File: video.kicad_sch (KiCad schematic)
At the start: 18 parts, among them Q1 BC547B, Q3 BC547B, Q4 BC547B, Q5 BC547B, Q6 BC547B

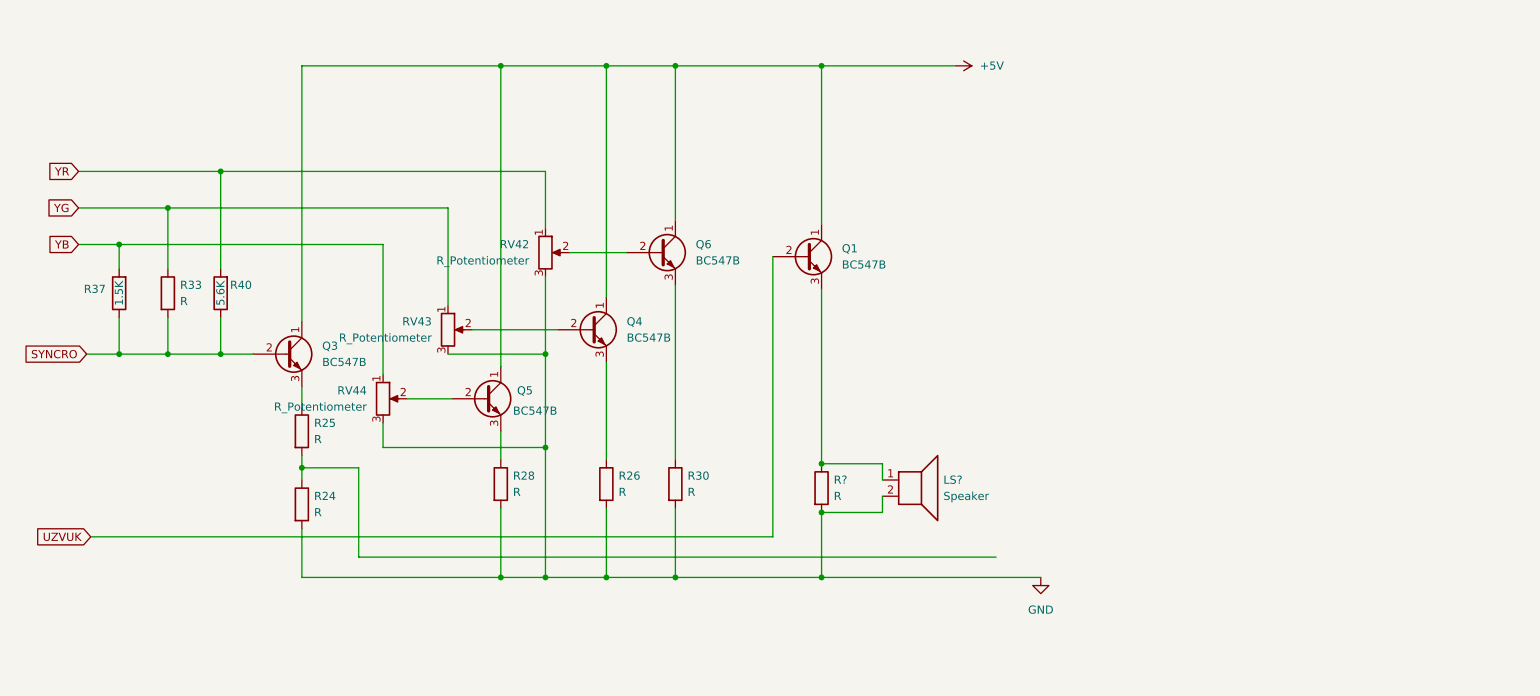
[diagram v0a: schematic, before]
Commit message: March 23rd First pre-alpha
First time ZERO errors and 93 warnings. Schematics are done, now to deal with warnings and footprints.
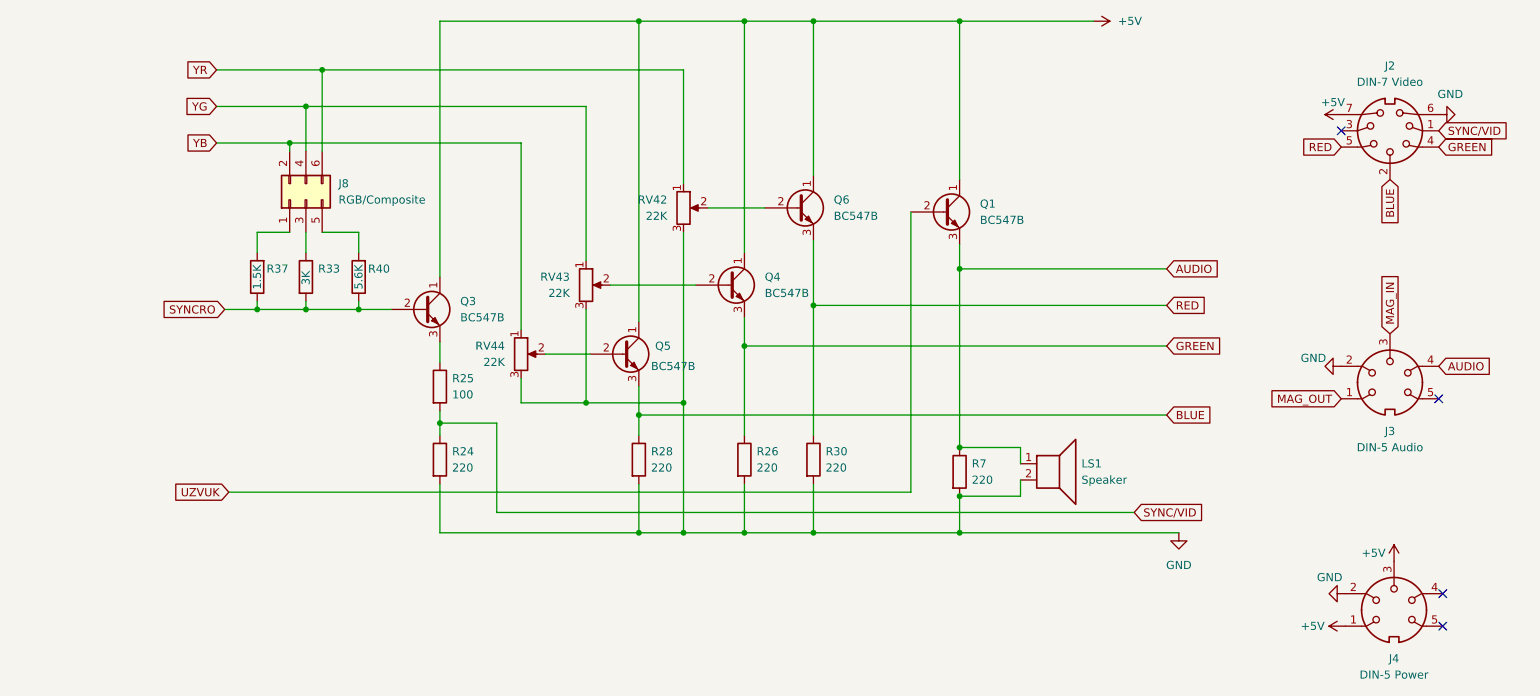
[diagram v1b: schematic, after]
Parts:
- added J2: DIN-7 Video, symbol Connector:DIN-7
- added J3: DIN-5 Audio, symbol Connector:DIN-5
- added J4: DIN-5 Power, symbol Connector:DIN-5
- added J8: RGB/Composite, Connector_PinHeader_2.54mm:PinHeader_2x03_P2.54mm_Vertical, symbol Connector_Generic:Conn_02x03_Odd_Even
- R24, R26, R28, R30: value R -> 220; footprint (none) -> Resistor_THT:R_Axial_DIN0207_L6.3mm_D2.5mm_P10.16mm_Horizontal
- R25: value R -> 100; footprint (none) -> Resistor_THT:R_Axial_DIN0207_L6.3mm_D2.5mm_P10.16mm_Horizontal
- R33: value R -> 3K; footprint (none) -> Resistor_THT:R_Axial_DIN0207_L6.3mm_D2.5mm_P10.16mm_Horizontal
- R37, R40: footprint (none) -> Resistor_THT:R_Axial_DIN0207_L6.3mm_D2.5mm_P10.16mm_Horizontal
- R7: renamed from R?; value R -> 220; footprint (none) -> Resistor_THT:R_Axial_DIN0207_L6.3mm_D2.5mm_P10.16mm_Horizontal
- RV42, RV43, RV44: value R_Potentiometer -> 22K
- gave numbers to parts that had none: 1
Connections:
- net +5V: now also J2.7, J4.1, J4.3
- net GND: now also J2.6, J3.2, J4.2
- net YB: now also J8.2 (Pin_2); no longer R37.2
- net YG: now also J8.4 (Pin_4); no longer R33.1
- net YR: now also J8.6 (Pin_6); no longer R40.2
- net SYNC/VID: now reaches R24.1, R25.2
- net SYNC/VID: now also J2.1
- net AUDIO: now reaches LS1.1, Q1.3 (E), R7.1
- net AUDIO: now also J3.4
- net BLUE: now reaches Q5.3 (E), R28.1
- net BLUE: now also J2.2
- net GREEN: now reaches Q4.3 (E), R26.1
- net GREEN: now also J2.4
- net RED: now reaches Q6.3 (E), R30.1
- net RED: now also J2.5
- new net: J8.5 (Pin_5), R40.2
- new net: J8.1 (Pin_1), R37.2
- new net: J8.3 (Pin_3), R33.1
- new net MAG_IN: J3.3
- new net MAG_OUT: J3.1
- no-connect marks 0 -> 4
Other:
- moved on the sheet: LS1, Q1, Q3, Q4, Q5, Q6, R24, R25, R26, R28, R30, R33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

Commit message: March 24th - First Edition of PCB
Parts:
- J3, J4: footprint (none) -> w_conn_av:din-5
- LS1: footprint (none) -> Connector_PinHeader_2.54mm:PinHeader_1x02_P2.54mm_Vertical
- RV42, RV43, RV44: footprint (none) -> Potentiometer_THT:Potentiometer_Bourns_PTV09A-2_Single_Horizontal
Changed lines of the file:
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@@
       (effects (font (size 1.27 1.27)) (justify right))
     )
-    (property "Footprint" "" (id 2) (at 137.795 80.01 0)
+    (property "Footprint" "Potentiometer_THT:Potentiometer_Bourns_PTV09A-2_Single_Horizontal" (id 2) (at 137.795 80.01 0)
       (effects (font (size 1.27 1.27)) hide)
     )
@@
       (effects (font (size 1.27 1.27)) (justify right))
     )
-    (property "Footprint" "" (id 2) (at 122.555 92.075 0)
+    (property "Footprint" "Potentiometer_THT:Potentiometer_Bourns_PTV09A-2_Single_Horizontal" (id 2) (at 122.555 92.075 0)
       (effects (font (size 1.27 1.27)) hide)
     )
@@
       (effects (font (size 1.27 1.27)) (justify left))
     )
-    (property "Footprint" "" (id 2) (at 195.58 125.095 0)
+    (property "Footprint" "Connector_PinHeader_2.54mm:PinHeader_1x02_P2.54mm_Vertical" (id 2) (at 195.58 125.095 0)
       (effects (font (size 1.27 1.27)) hide)
     )
@@
     (property "Reference" "J3" (id 0) (at 248.2851 114.935 0))
     (property "Value" "DIN-5 Audio" (id 1) (at 248.2851 117.475 0))
-    (property "Footprint" "" (id 2) (at 248.285 107.315 0)
+    (property "Footprint" "w_conn_av:din-5" (id 2) (at 248.285 107.315 0)
       (effects (font (size 1.27 1.27)) hide)
     )
@@
     (property "Reference" "J4" (id 0) (at 248.9201 150.495 0))
     (property "Value" "DIN-5 Power" (id 1) (at 248.9201 153.035 0))
-    (property "Footprint" "" (id 2) (at 248.92 142.875 0)
+    (property "Footprint" "w_conn_av:din-5" (id 2) (at 248.92 142.875 0)
       (effects (font (size 1.27 1.27)) hide)
     )
@@
       (effects (font (size 1.27 1.27)) (justify right))
     )
-    (property "Footprint" "" (id 2) (at 112.395 102.87 0)
-      (effects (font (size 1.27 1.27)) hide)
-    )
+    (property "Footprint" "Potentiometer_THT:Potentiometer_Bourns_PTV09A-2_Single_Horizontal" (id 2) (at 112.395 102.87 0)
+      (effects (font (size 1.27 1.27)) hide)
+    )

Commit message: March 26th update
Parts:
- J2: footprint (none) -> w_conn_av:DIN-7-Variable
- J3, J4: footprint w_conn_av:din-5 -> w_conn_av:DIN-5-Variable
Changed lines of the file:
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@@
     (property "Reference" "J2" (id 0) (at 248.2849 57.785 0))
     (property "Value" "DIN-7 Video" (id 1) (at 248.2849 60.325 0))
-    (property "Footprint" "" (id 2) (at 248.285 67.945 0)
+    (property "Footprint" "w_conn_av:DIN-7-Variable" (id 2) (at 248.285 67.945 0)
       (effects (font (size 1.27 1.27)) hide)
     )
@@
     (property "Reference" "J3" (id 0) (at 248.2851 114.935 0))
     (property "Value" "DIN-5 Audio" (id 1) (at 248.2851 117.475 0))
-    (property "Footprint" "w_conn_av:din-5" (id 2) (at 248.285 107.315 0)
+    (property "Footprint" "w_conn_av:DIN-5-Variable" (id 2) (at 248.285 107.315 0)
       (effects (font (size 1.27 1.27)) hide)
     )
@@
     (property "Reference" "J4" (id 0) (at 248.9201 150.495 0))
     (property "Value" "DIN-5 Power" (id 1) (at 248.9201 153.035 0))
-    (property "Footprint" "w_conn_av:din-5" (id 2) (at 248.92 142.875 0)
+    (property "Footprint" "w_conn_av:DIN-5-Variable" (id 2) (at 248.92 142.875 0)
       (effects (font (size 1.27 1.27)) hide)
     )

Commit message: 28th march ver2
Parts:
- RV42, RV43, RV44: footprint Potentiometer_THT:Potentiometer_Bourns_PTV09A-2_Single_Horizontal -> Potentiometer_THT:Potentiometer_Bourns_3299X_Horizontal
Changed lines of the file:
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@@
       (effects (font (size 1.27 1.27)) (justify right))
     )
-    (property "Footprint" "Potentiometer_THT:Potentiometer_Bourns_PTV09A-2_Single_Horizontal" (id 2) (at 137.795 80.01 0)
+    (property "Footprint" "Potentiometer_THT:Potentiometer_Bourns_3299X_Horizontal" (id 2) (at 137.795 80.01 0)
       (effects (font (size 1.27 1.27)) hide)
     )
@@
       (effects (font (size 1.27 1.27)) (justify right))
     )
-    (property "Footprint" "Potentiometer_THT:Potentiometer_Bourns_PTV09A-2_Single_Horizontal" (id 2) (at 122.555 92.075 0)
+    (property "Footprint" "Potentiometer_THT:Potentiometer_Bourns_3299X_Horizontal" (id 2) (at 122.555 92.075 0)
       (effects (font (size 1.27 1.27)) hide)
     )
@@
       (effects (font (size 1.27 1.27)) (justify right))
     )
-    (property "Footprint" "Potentiometer_THT:Potentiometer_Bourns_PTV09A-2_Single_Horizontal" (id 2) (at 112.395 102.87 0)
-      (effects (font (size 1.27 1.27)) hide)
-    )
+    (property "Footprint" "Potentiometer_THT:Potentiometer_Bourns_3299X_Horizontal" (id 2) (at 112.395 102.87 0)
+      (effects (font (size 1.27 1.27)) hide)
+    )
